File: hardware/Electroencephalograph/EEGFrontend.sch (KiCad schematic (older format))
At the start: 80 parts

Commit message: paritial routing for analog part
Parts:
- added J1: Conn_01x08_Male, Connector_PinHeader_2.54mm:PinHeader_1x08_P2.54mm_Horizontal, symbol Connector:Conn_01x08_Male
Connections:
- net labels added: A_GND, A_VDD, A_VSS, ECC_1, ECC_2, ECC_3, ECC_4, ECC_5, ECC_6, ECC_7, ECC_8, ELECTRODE_1, ELECTRODE_2, ELECTRODE_3, ELECTRODE_4, ELECTRODE_5, ELECTRODE_6, ELECTRODE_7, ELECTRODE_8
- net labels removed: GNDA, VDDA
- wire segments 240 -> 214
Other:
- moved on the sheet: C1, C10, C11, C12, C13, C14, C15, C16, C17, C18, C19, C2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

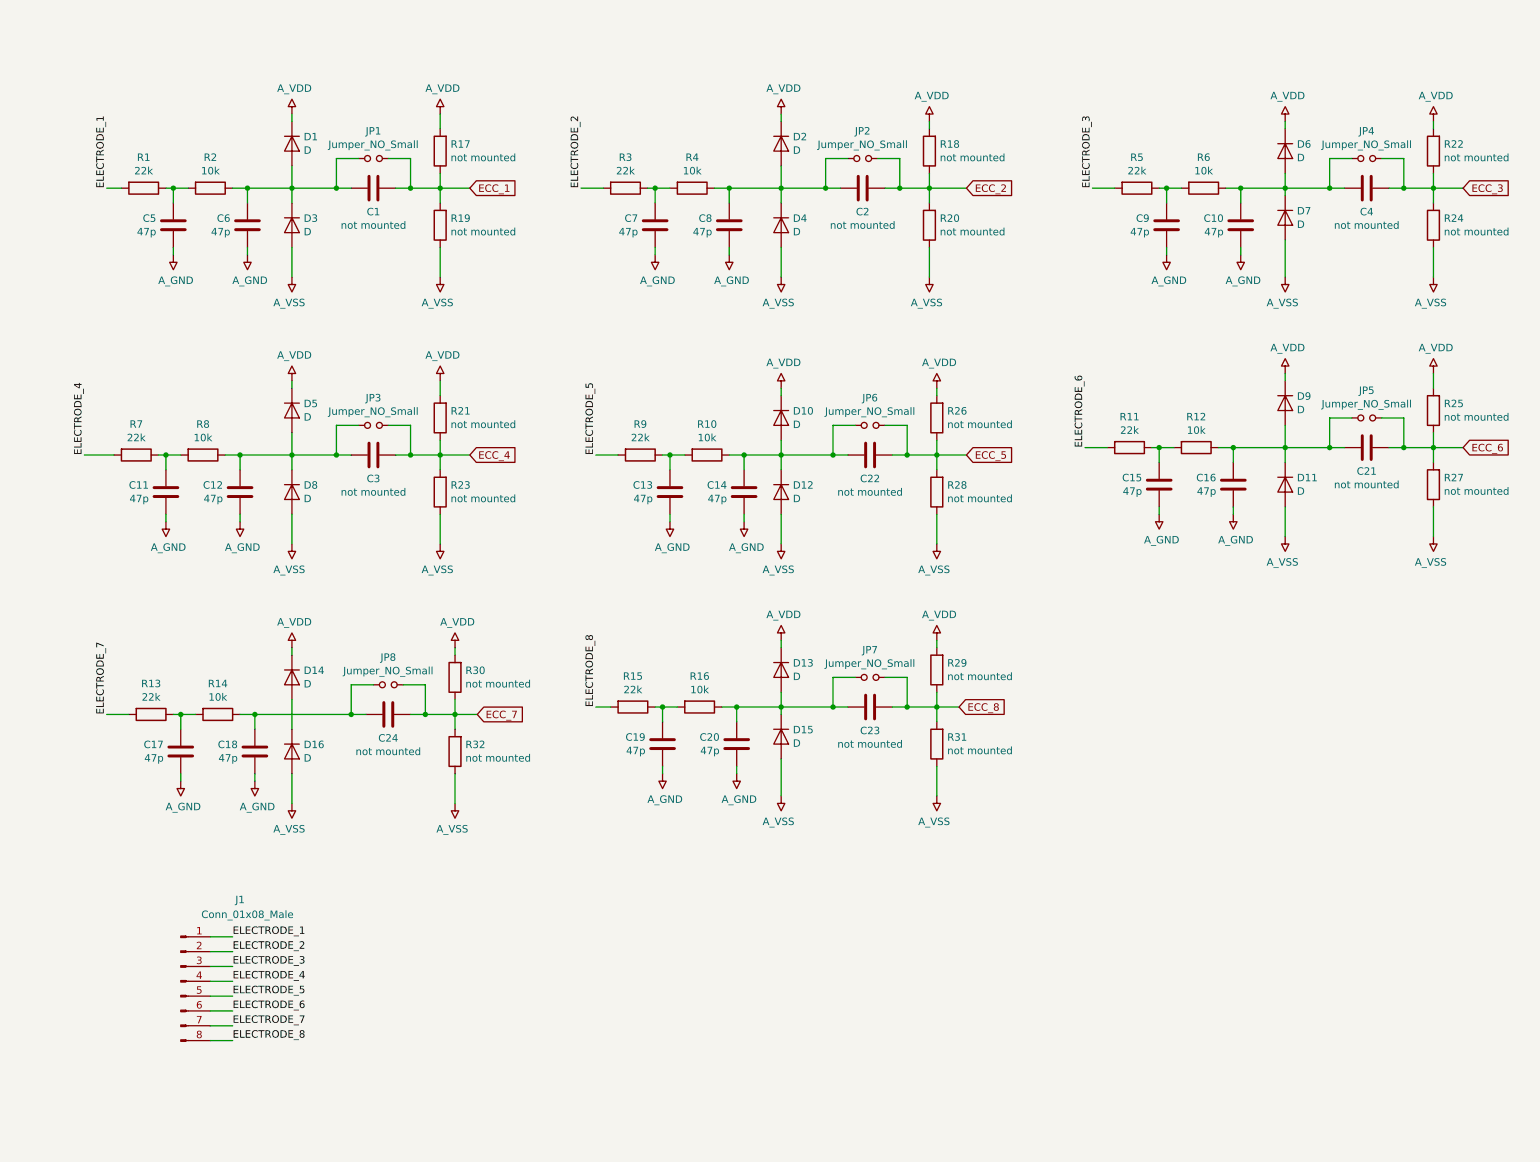
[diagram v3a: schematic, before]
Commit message: removed external clk and vref
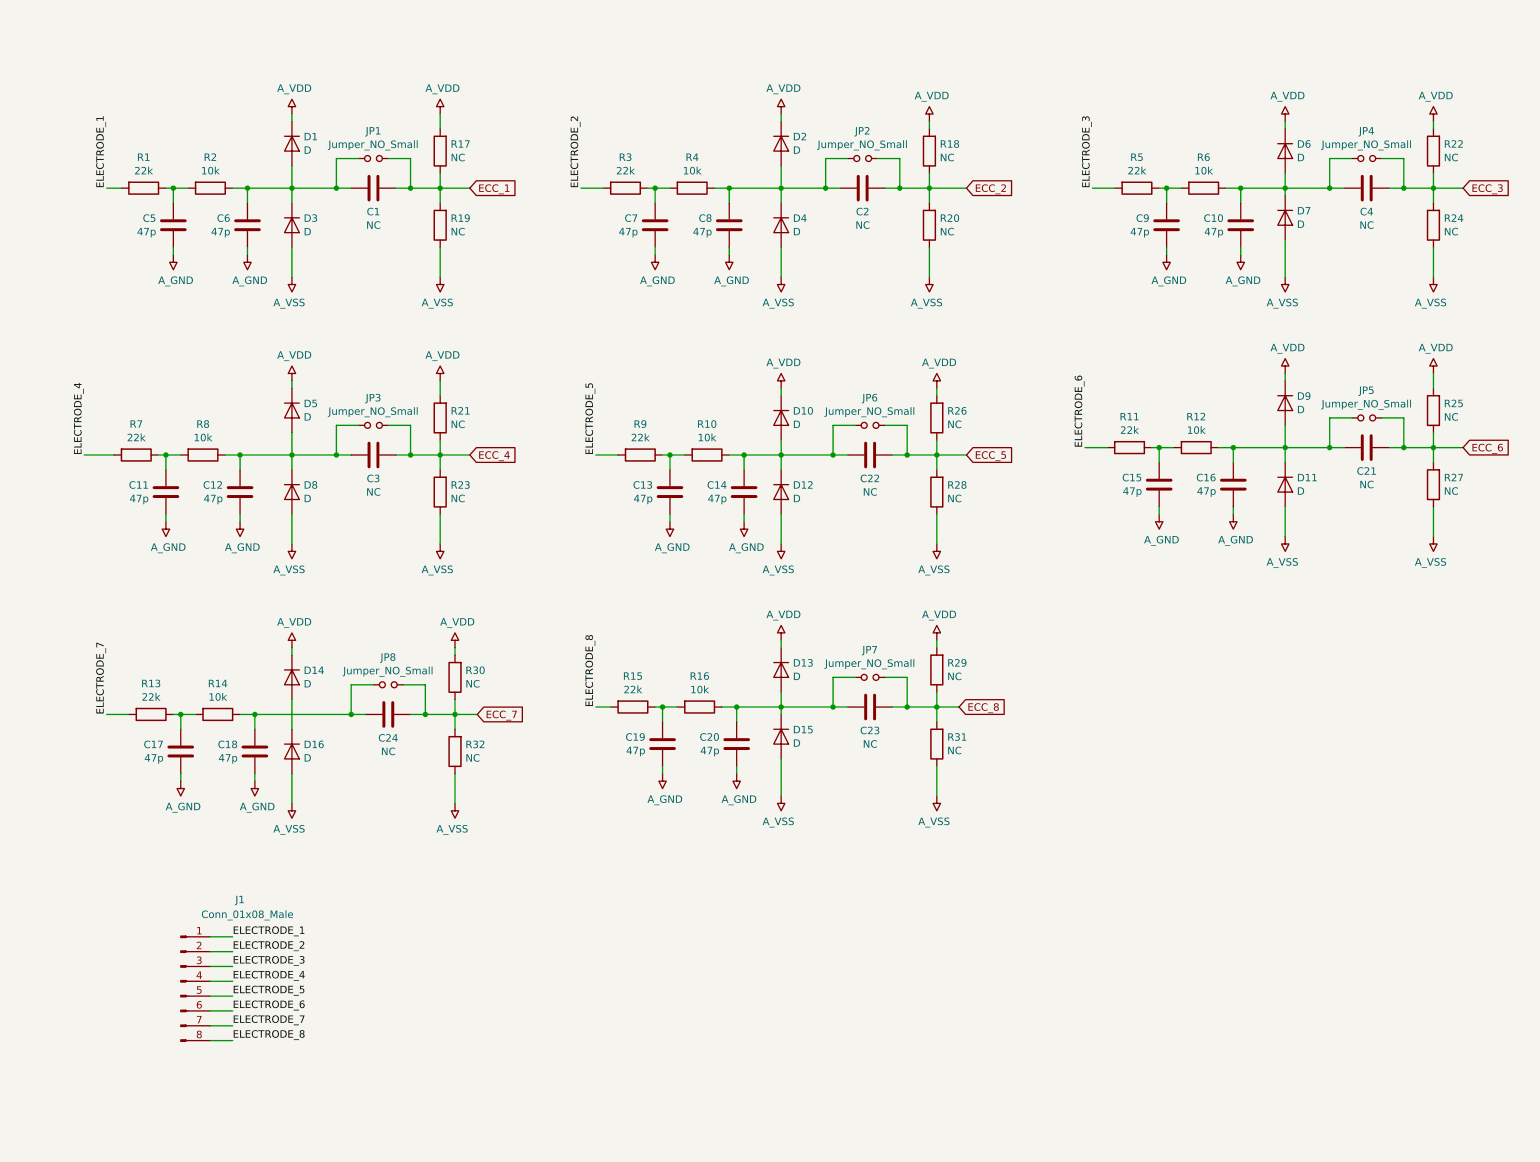
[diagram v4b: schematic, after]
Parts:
- C1, C2, C21, C22, C23, C24, C3, C4, R17, R18, R19, R20, R21, R22, R23, R24, R25, R26, R27, R28, R29, R30, R31, R32: value not mounted -> NC
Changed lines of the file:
@@
 P 3000 1550
 F 0 "C1" V 2840 1550 50  0000 C CNN
-F 1 "not mounted" V 2749 1550 50  0000 C CNN
+F 1 "NC" V 2749 1550 50  0000 C CNN
 F 2 "Capacitor_SMD:C_0402_1005Metric" H 3038 1400 50  0001 C CNN
 F 3 "~" H 3000 1550 50  0001 C CNN
@@
 AR Path="/5DF4CFF8/5DFBB024" Ref="R17"  Part="1"
 F 0 "R17" H 3380 1254 50  0000 R CNN
-F 1 "not mounted" H 3380 1345 50  0000 R CNN
+F 1 "NC" H 3380 1345 50  0000 R CNN
 F 2 "Resistor_SMD:R_0402_1005Metric" V 3380 1300 50  0001 C CNN
 F 3 "~" H 3450 1300 50  0001 C CNN
@@
 AR Path="/5DF4CFF8/5DFBB639" Ref="R19"  Part="1"
 F 0 "R19" H 3380 1754 50  0000 R CNN
-F 1 "not mounted" H 3380 1845 50  0000 R CNN
+F 1 "NC" H 3380 1845 50  0000 R CNN
 F 2 "Resistor_SMD:R_0402_1005Metric" V 3380 1800 50  0001 C CNN
 F 3 "~" H 3450 1800 50  0001 C CNN
@@
 P 9700 1550
 F 0 "C4" V 9540 1550 50  0000 C CNN
-F 1 "not mounted" V 9449 1550 50  0000 C CNN
+F 1 "NC" V 9449 1550 50  0000 C CNN
 F 2 "Capacitor_SMD:C_0402_1005Metric" H 9738 1400 50  0001 C CNN
 F 3 "~" H 9700 1550 50  0001 C CNN
@@
 AR Path="/5DF4CFF8/5E0624CB" Ref="R22"  Part="1"
 F 0 "R22" H 10080 1254 50  0000 R CNN
-F 1 "not mounted" H 10080 1345 50  0000 R CNN
+F 1 "NC" H 10080 1345 50  0000 R CNN
 F 2 "Resistor_SMD:R_0402_1005Metric" V 10080 1300 50  0001 C CNN
 F 3 "~" H 10150 1300 50  0001 C CNN
@@
 AR Path="/5DF4CFF8/5E0624D1" Ref="R24"  Part="1"
 F 0 "R24" H 10080 1754 50  0000 R CNN
-F 1 "not mounted" H 10080 1845 50  0000 R CNN
+F 1 "NC" H 10080 1845 50  0000 R CNN
 F 2 "Resistor_SMD:R_0402_1005Metric" V 10080 1800 50  0001 C CNN
 F 3 "~" H 10150 1800 50  0001 C CNN
@@
 P 6350 3350
 F 0 "C22" V 6190 3350 50  0000 C CNN
-F 1 "not mounted" V 6099 3350 50  0000 C CNN
+F 1 "NC" V 6099 3350 50  0000 C CNN
 F 2 "Capacitor_SMD:C_0402_1005Metric" H 6388 3200 50  0001 C CNN
 F 3 "~" H 6350 3350 50  0001 C CNN
@@
 AR Path="/5DF4CFF8/5E06E5C0" Ref="R26"  Part="1"
 F 0 "R26" H 6730 3054 50  0000 R CNN
-F 1 "not mounted" H 6730 3145 50  0000 R CNN
+F 1 "NC" H 6730 3145 50  0000 R CNN
 F 2 "Resistor_SMD:R_0402_1005Metric" V 6730 3100 50  0001 C CNN
 F 3 "~" H 6800 3100 50  0001 C CNN
@@
 P 3100 5100
 F 0 "C24" V 2940 5100 50  0000 C CNN
-F 1 "not mounted" V 2849 5100 50  0000 C CNN
+F 1 "NC" V 2849 5100 50  0000 C CNN
 F 2 "Capacitor_SMD:C_0402_1005Metric" H 3138 4950 50  0001 C CNN
 F 3 "~" H 3100 5100 50  0001 C CNN
@@
 AR Path="/5DF4CFF8/5E07C84A" Ref="R30"  Part="1"
 F 0 "R30" H 3480 4804 50  0000 R CNN
-F 1 "not mounted" H 3480 4895 50  0000 R CNN
+F 1 "NC" H 3480 4895 50  0000 R CNN
 F 2 "Resistor_SMD:R_0402_1005Metric" V 3480 4850 50  0001 C CNN
 F 3 "~" H 3550 4850 50  0001 C CNN
@@
 AR Path="/5DF4CFF8/5E07C850" Ref="R32"  Part="1"
 F 0 "R32" H 3480 5304 50  0000 R CNN
-F 1 "not mounted" H 3480 5395 50  0000 R CNN
+F 1 "NC" H 3480 5395 50  0000 R CNN
 F 2 "Resistor_SMD:R_0402_1005Metric" V 3480 5350 50  0001 C CNN
 F 3 "~" H 3550 5350 50  0001 C CNN
@@
 P 6300 1550
 F 0 "C2" V 6140 1550 50  0000 C CNN
-F 1 "not mounted" V 6049 1550 50  0000 C CNN
+F 1 "NC" V 6049 1550 50  0000 C CNN
 F 2 "Capacitor_SMD:C_0402_1005Metric" H 6338 1400 50  0001 C CNN
 F 3 "~" H 6300 1550 50  0001 C CNN
@@
 AR Path="/5DF4CFF8/5E08DA93" Ref="R18"  Part="1"
 F 0 "R18" H 6680 1254 50  0000 R CNN
-F 1 "not mounted" H 6680 1345 50  0000 R CNN
+F 1 "NC" H 6680 1345 50  0000 R CNN
 F 2 "Resistor_SMD:R_0402_1005Metric" V 6680 1300 50  0001 C CNN
 F 3 "~" H 6750 1300 50  0001 C CNN
@@
 AR Path="/5DF4CFF8/5E08DA99" Ref="R20"  Part="1"
 F 0 "R20" H 6680 1754 50  0000 R CNN
-F 1 "not mounted" H 6680 1845 50  0000 R CNN
+F 1 "NC" H 6680 1845 50  0000 R CNN
 F 2 "Resistor_SMD:R_0402_1005Metric" V 6680 1800 50  0001 C CNN
 F 3 "~" H 6750 1800 50  0001 C CNN
@@
 P 3000 3350
 F 0 "C3" V 2840 3350 50  0000 C CNN
-F 1 "not mounted" V 2749 3350 50  0000 C CNN
+F 1 "NC" V 2749 3350 50  0000 C CNN
 F 2 "Capacitor_SMD:C_0402_1005Metric" H 3038 3200 50  0001 C CNN
 F 3 "~" H 3000 3350 50  0001 C CNN
@@
 AR Path="/5DF4CFF8/5E09D94A" Ref="R21"  Part="1"
 F 0 "R21" H 3380 3054 50  0000 R CNN
-F 1 "not mounted" H 3380 3145 50  0000 R CNN
+F 1 "NC" H 3380 3145 50  0000 R CNN
 F 2 "Resistor_SMD:R_0402_1005Metric" V 3380 3100 50  0001 C CNN
 F 3 "~" H 3450 3100 50  0001 C CNN
@@
 AR Path="/5DF4CFF8/5E09D950" Ref="R23"  Part="1"
 F 0 "R23" H 3380 3554 50  0000 R CNN
-F 1 "not mounted" H 3380 3645 50  0000 R CNN
+F 1 "NC" H 3380 3645 50  0000 R CNN
 F 2 "Resistor_SMD:R_0402_1005Metric" V 3380 3600 50  0001 C CNN
 F 3 "~" H 3450 3600 50  0001 C CNN
@@
 P 9700 3300
 F 0 "C21" V 9540 3300 50  0000 C CNN
-F 1 "not mounted" V 9449 3300 50  0000 C CNN
+F 1 "NC" V 9449 3300 50  0000 C CNN
 F 2 "Capacitor_SMD:C_0402_1005Metric" H 9738 3150 50  0001 C CNN
 F 3 "~" H 9700 3300 50  0001 C CNN
@@
 AR Path="/5DF4CFF8/5E0AEAE6" Ref="R25"  Part="1"
 F 0 "R25" H 10080 3004 50  0000 R CNN
-F 1 "not mounted" H 10080 3095 50  0000 R CNN
+F 1 "NC" H 10080 3095 50  0000 R CNN
 F 2 "Resistor_SMD:R_0402_1005Metric" V 10080 3050 50  0001 C CNN
 F 3 "~" H 10150 3050 50  0001 C CNN
@@
 AR Path="/5DF4CFF8/5E0AEAEC" Ref="R27"  Part="1"
 F 0 "R27" H 10080 3504 50  0000 R CNN
-F 1 "not mounted" H 10080 3595 50  0000 R CNN
+F 1 "NC" H 10080 3595 50  0000 R CNN
 F 2 "Resistor_SMD:R_0402_1005Metric" V 10080 3550 50  0001 C CNN
 F 3 "~" H 10150 3550 50  0001 C CNN
@@
 P 6350 5050
 F 0 "C23" V 6190 5050 50  0000 C CNN
-F 1 "not mounted" V 6099 5050 50  0000 C CNN
+F 1 "NC" V 6099 5050 50  0000 C CNN
 F 2 "Capacitor_SMD:C_0402_1005Metric" H 6388 4900 50  0001 C CNN
 F 3 "~" H 6350 5050 50  0001 C CNN
@@
 AR Path="/5DF4CFF8/5E0C1192" Ref="R29"  Part="1"
 F 0 "R29" H 6730 4754 50  0000 R CNN
-F 1 "not mounted" H 6730 4845 50  0000 R CNN
+F 1 "NC" H 6730 4845 50  0000 R CNN
 F 2 "Resistor_SMD:R_0402_1005Metric" V 6730 4800 50  0001 C CNN
 F 3 "~" H 6800 4800 50  0001 C CNN
@@
 AR Path="/5DF4CFF8/5E0C1198" Ref="R31"  Part="1"
 F 0 "R31" H 6730 5254 50  0000 R CNN
-F 1 "not mounted" H 6730 5345 50  0000 R CNN
+F 1 "NC" H 6730 5345 50  0000 R CNN
 F 2 "Resistor_SMD:R_0402_1005Metric" V 6730 5300 50  0001 C CNN
 F 3 "~" H 6800 5300 50  0001 C CNN
@@
 AR Path="/5DF4CFF8/5E06E5C6" Ref="R28"  Part="1"
 F 0 "R28" H 6730 3554 50  0000 R CNN
-F 1 "not mounted" H 6730 3645 50  0000 R CNN
+F 1 "NC" H 6730 3645 50  0000 R CNN
 F 2 "Resistor_SMD:R_0402_1005Metric" V 6730 3600 50  0001 C CNN
 F 3 "~" H 6800 3600 50  0001 C CNN
